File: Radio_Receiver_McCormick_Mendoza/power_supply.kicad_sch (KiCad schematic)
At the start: 31 parts, among them J1 VBAT, J2 GND, J23 VDDA, J26 +5V, J3 VA_3.3, J36 +5V RAW, J37 V_4.8, J39 VDD, J4 VA_4.8, J6 Conn_01x02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

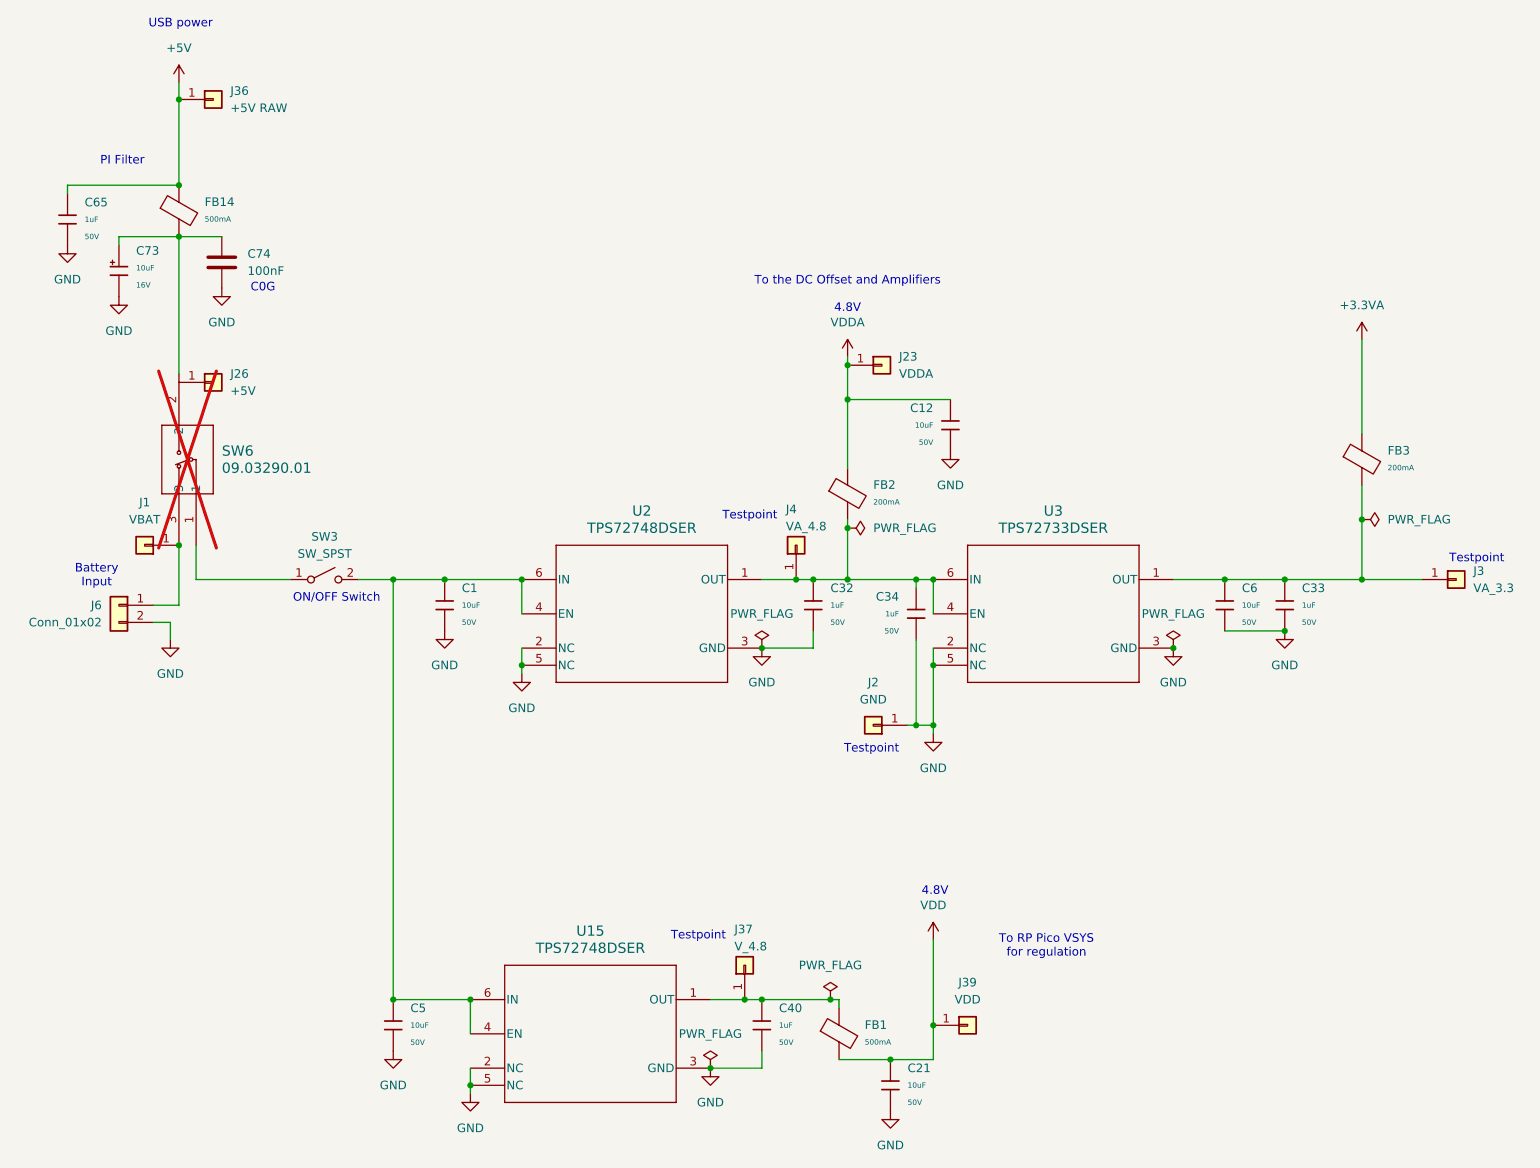
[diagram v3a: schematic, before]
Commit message: Swapped voltage regulator to output 4.5V
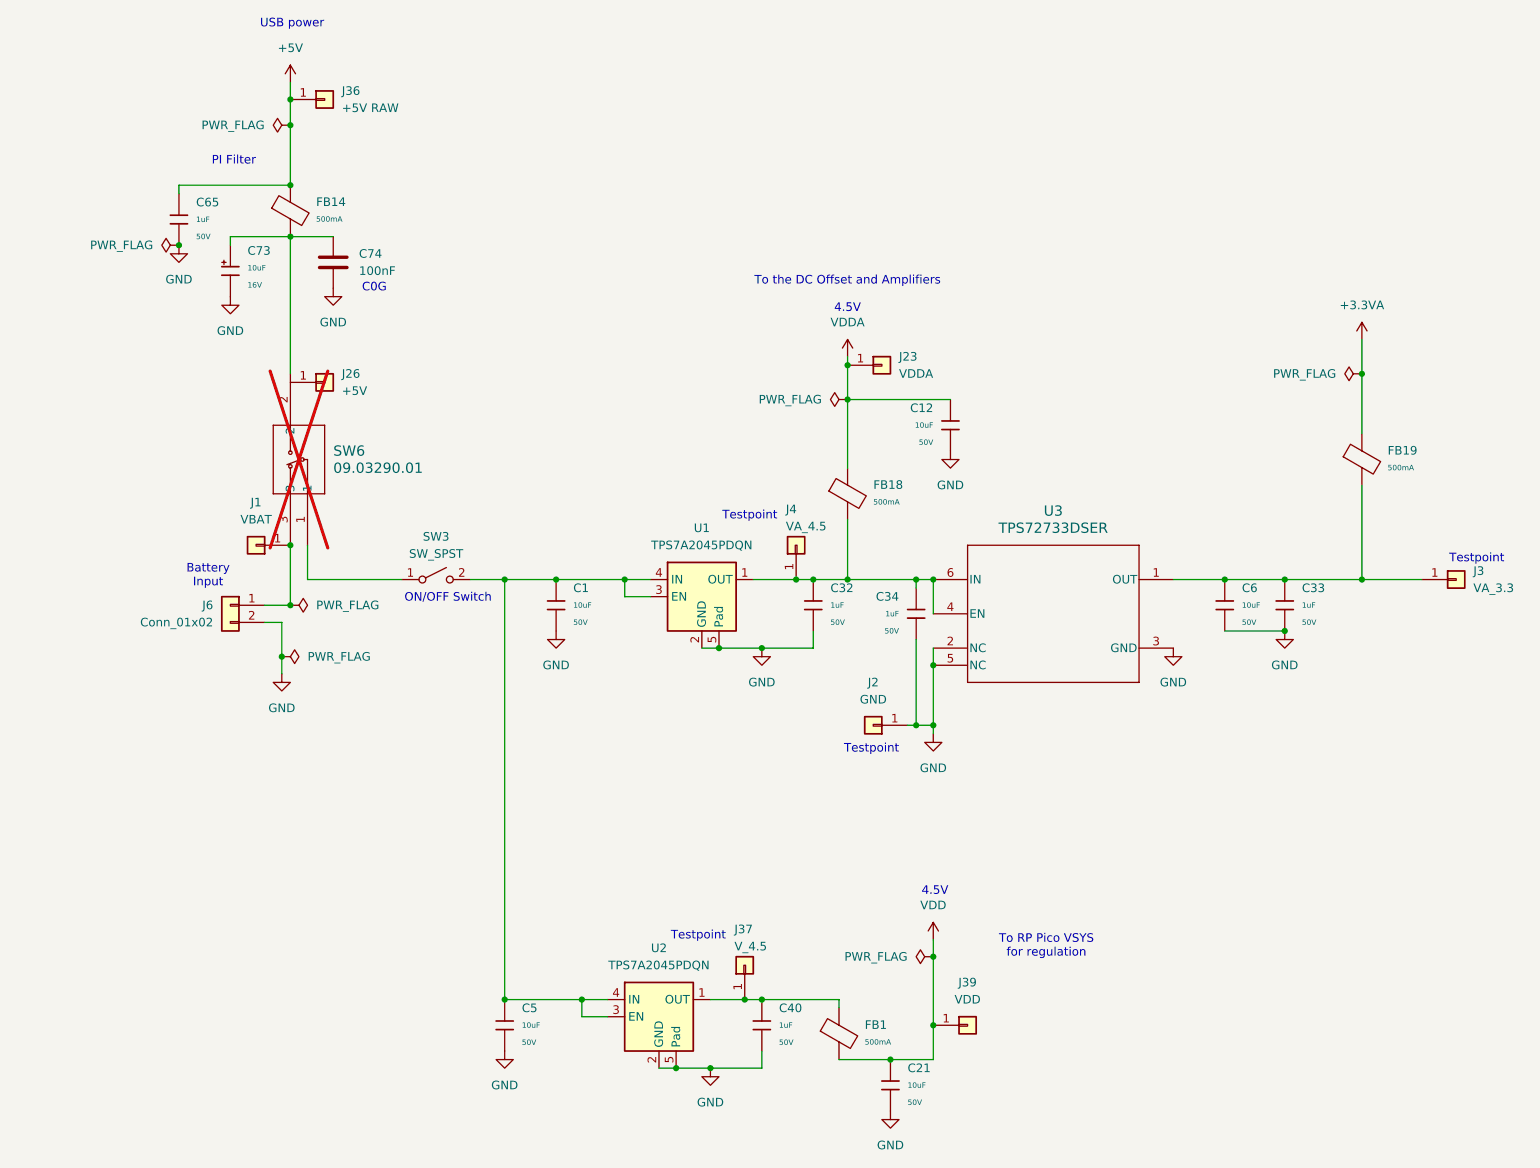
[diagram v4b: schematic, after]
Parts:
- removed FB2, FB3: (no value), PCM_JLCPCB:FB_0603, symbol PCM_JLCPCB-Inductors:Ferrite,0603
- removed U15, U2: TPS72748DSER, TPS727-4.8V_regulator:DSE0006A, symbol 2026-04-20_23-44-26:TPS72748DSER
- added FB18, FB19: (no value), PCM_JLCPCB:FB_0805, symbol PCM_JLCPCB-Inductors:Ferrite,0805,(2)
- added U1, U2: TPS7A2045PDQN, Package_SON:Texas_X2SON-4_1x1mm_P0.65mm, symbol Regulator_Linear:TPS7A20xxxDQN
- J37: value V_4.8 -> V_4.5
- J4: value VA_4.8 -> VA_4.5
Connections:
- net +3.3VA: now also FB19.1
- net GND: now also U1.2 (GND), U1.5 (Pad), U2.2 (GND), U2.5 (Pad)
- net VDDA: now also FB18.1
- net at C32.1, C34.2, J4.1 (Pin_1)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: now also FB18.2, U1.1 (OUT)
- net at C1.1, C5.1, SW3.2 (B): now also U1.3 (EN), U1.4 (IN), U2.3 (EN), U2.4 (IN)
- net at C40.1, FB1.1, J37.1 (Pin_1): now also U2.1 (OUT)
- net at C33.1, C6.1, J3.1 (Pin_1)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: now also FB19.2
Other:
- note added: "4.5V"
- note removed: "4.8V"
- moved on the sheet: C1, C5, C65, C73, C74, FB14, J1, J26, J36, J6, SW3, SW6

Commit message: Added MicroSD card and verified footprints
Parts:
- removed SW3: SW_SPST, symbol Switch:SW_SPST
- added ON/OFF: 09.03290.01, SWITCH SLIDE SPDT 0.5A 24V 09.03290.01:09.03290_EAO, symbol SWITCH SLIDE SPDT 0.5A 24V 09.03290.01:09.03290.01
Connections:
- net at C1.1, C5.1, U1.3 (EN)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: now also ON/OFF.3
- net at SW6.1: now also ON/OFF.1
- no-connect marks 0 -> 1
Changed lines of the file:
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@@
 	(text "ON/OFF Switch\n"
 		(exclude_from_sim no)
-		(at 83.058 104.394 0)
+		(at 83.566 104.394 0)
 		(effects
 			(font
@@
 		(color 0 0 0 0)
 	)
+	(no_connect
+		(at 86.36 76.2)
+	)
 	(wire
 		(pts
@@
 	(wire
 		(pts
-			(xy 62.23 101.6) (xy 76.2 101.6)
+			(xy 62.23 101.6) (xy 83.82 101.6)
 		)
 		(stroke
@@
 	)
 	(symbol
+		(lib_id "SWITCH SLIDE SPDT 0.5A 24V 09.03290.01:09.03290.01")
+		(at 86.36 76.2 270)
+		(unit 1)
+		(body_style 1)
+		(exclude_from_sim no)
+		(in_bom yes)
+		(on_board yes)
+		(in_pos_files yes)
+		(dnp yes)
+		(property "Reference" "ON/OFF"
+			(at 90.17 90.1701 90)
+			(show_name no)
+			(do_not_autoplace no)
+			(effects
+				(font
+					(size 1.524 1.524)
+				)
+				(justify left)
+			)
+		)
+		(property "Value" "09.03290.01"
+			(at 90.17 87.6301 90)
+			(show_name no)
+			(do_not_autoplace no)
+			(effects
+				(font
+					(size 1.524 1.524)
+				)
+				(justify left)
+			)
+		)
+		(property "Footprint" "SWITCH SLIDE SPDT 0.5A 24V 09.03290.01:09.03290_EAO"
+			(at 86.36 76.2 0)
+			(hide yes)
+			(show_name no)
+			(do_not_autoplace no)
+			(effects
+				(font
+					(size 1.27 1.27)
+					(italic yes)
+				)
+			)
+		)
+		(property "Datasheet" "https://mm.digikey.com/Volume0/opasdata/d220001/medias/docus/496/series1k2_201004.pdf"
+			(at 86.36 76.2 0)
+			(hide yes)
+			(show_name no)
+			(do_not_autoplace no)
+			(effects
+				(font
+					(size 1.27 1.27)
+					(italic yes)
+				)
+			)
+		)
+		(property "Description" "Slide Switch SPDT Through Hole"
+			(at 86.36 76.2 0)
+			(hide yes)
+			(show_name no)
+			(do_not_autoplace no)
+			(effects
+				(font
+					(size 1.27 1.27)
+				)
+			)
+		)
+		(pin "2"
+		)
+		(pin "1"
+		)
+		(pin "3"
+		)
+		(instances
+			(project "Radio_Receiver_McCormick_Mendoza"
+				(path "/f31d31ab-6846-4f3a-92b1-aa5a6a13373f/89503fbf-50e2-456e-a9ae-3607dd041f50"
+					(reference "ON/OFF")
+					(unit 1)
+				)
+			)
+		)
+	)
+	(symbol
 		(lib_id "PCM_JLCPCB-Inductors:Ferrite,0805,(2)")
 		(at 142.24 88.9 0)
@@
 					(unit 1)
 				)
-			)
-		)
-	)
-	(symbol
-		(lib_id "Switch:SW_SPST")
-		(at 81.28 101.6 0)
-		(unit 1)
-		(body_style 1)
-		(exclude_from_sim no)
-		(in_bom yes)
-		(on_board yes)
-		(in_pos_files yes)
-		(dnp no)
-		(fields_autoplaced yes)
-		(property "Reference" "SW3"
-			(at 81.28 95.25 0)
-			(show_name no)
-			(do_not_autoplace no)
-			(effects
-				(font
-					(size 1.27 1.27)
-				)
-			)
-		)
-		(property "Value" "SW_SPST"
-			(at 81.28 97.79 0)
-			(show_name no)
-			(do_not_autoplace no)
-			(effects
-				(font
-					(size 1.27 1.27)
-				)
-			)
-		)
-		(property "Footprint" ""
-			(at 81.28 101.6 0)
-			(hide yes)
-			(show_name no)
-			(do_not_autoplace no)
-			(effects
-				(font
-					(size 1.27 1.27)
-				)
-			)
-		)
-		(property "Datasheet" ""
-			(at 81.28 101.6 0)
-			(hide yes)
-			(show_name no)
-			(do_not_autoplace no)
-			(effects
-				(font
-					(size 1.27 1.27)
-				)
-			)
-		)
-		(property "Description" "Single Pole Single Throw (SPST) switch"
-			(at 81.28 101.6 0)
-			(hide yes)
-			(show_name no)
-			(do_not_autoplace no)
-			(effects
-				(font
-					(size 1.27 1.27)
-				)
-			)
-		)
-		(pin "2"
-		)
-		(pin "1"
-		)
-		(instances
-			(project "Radio_Receiver_McCormick_Mendoza"
-				(path "/f31d31ab-6846-4f3a-92b1-aa5a6a13373f/89503fbf-50e2-456e-a9ae-3607dd041f50"
-					(reference "SW3")
-					(unit 1)
-				)

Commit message: Updated footprints
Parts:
- renumbered ON/OFF to ON/OFF1
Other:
- note added: "POWER Switch"
- note removed: "ON/OFF Switch"
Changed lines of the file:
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@@
 		)
 	)
-	(text "ON/OFF Switch\n"
+	(text "POWER Switch\n"
 		(exclude_from_sim no)
 		(at 83.566 104.394 0)
@@
 		(in_pos_files yes)
 		(dnp yes)
-		(property "Reference" "ON/OFF"
+		(property "Reference" "ON/OFF1"
 			(at 90.17 90.1701 90)
 			(show_name no)
@@
 			(project "Radio_Receiver_McCormick_Mendoza"
 				(path "/f31d31ab-6846-4f3a-92b1-aa5a6a13373f/89503fbf-50e2-456e-a9ae-3607dd041f50"
-					(reference "ON/OFF")
+					(reference "ON/OFF1")
 					(unit 1)
 				)
